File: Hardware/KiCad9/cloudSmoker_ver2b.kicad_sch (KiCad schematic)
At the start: 54 parts, among them J1 AudioJack2_SwitchT, J10 Conn_01x02_Pin, J11 Conn_01x02_Pin, J12 Conn_01x02_Pin, J2 AudioJack2_SwitchT, J3 AudioJack2_SwitchT, J4 AudioJack2_SwitchT, J5 Conn_01x02_Pin, J6 Conn_01x02_Pin, J7 Conn_01x02_Pin, J8 Conn_01x02_Pin, J9 Conn_01x02_Pin, Q1 BSS138, Q2 BSS138, SW1 TS-1088-AR02016, SW2 TS-1088-AR02016, U1 SRV05-4-P-T7, U2 GT-USB-7010ASV, U3 ESP32-C3-WROOM-02U-N4, U4 AMS1117-3_3, U5 SRV05-4-P-T7, U6 ADS1115IRUGR

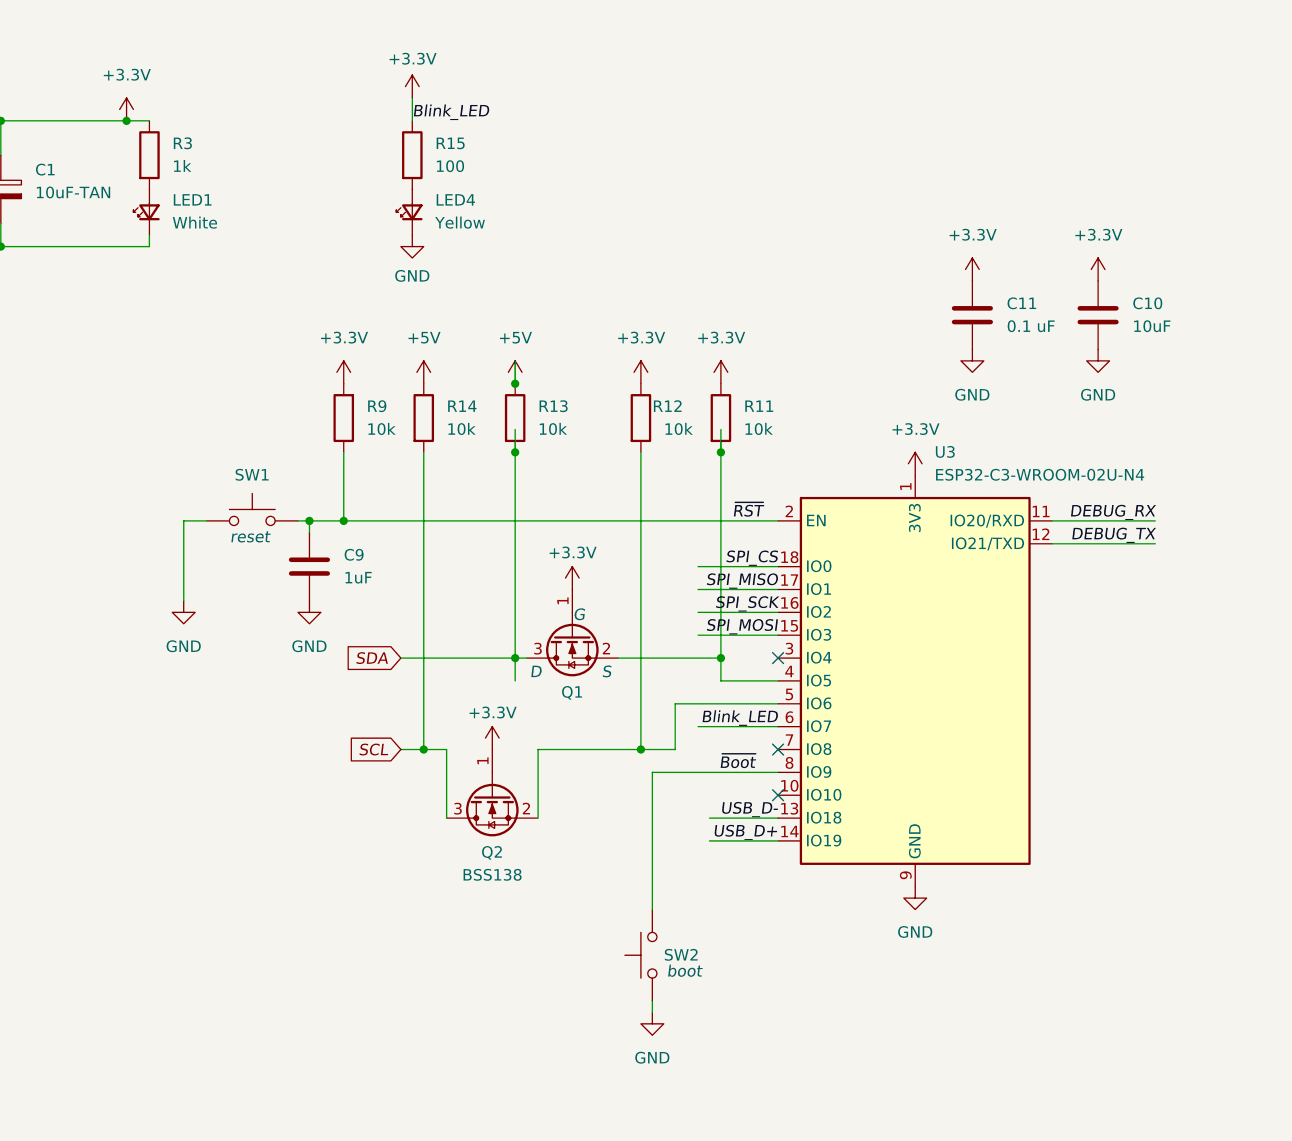
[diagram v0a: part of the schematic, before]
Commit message: cloudSmoker schematic ver2b changes
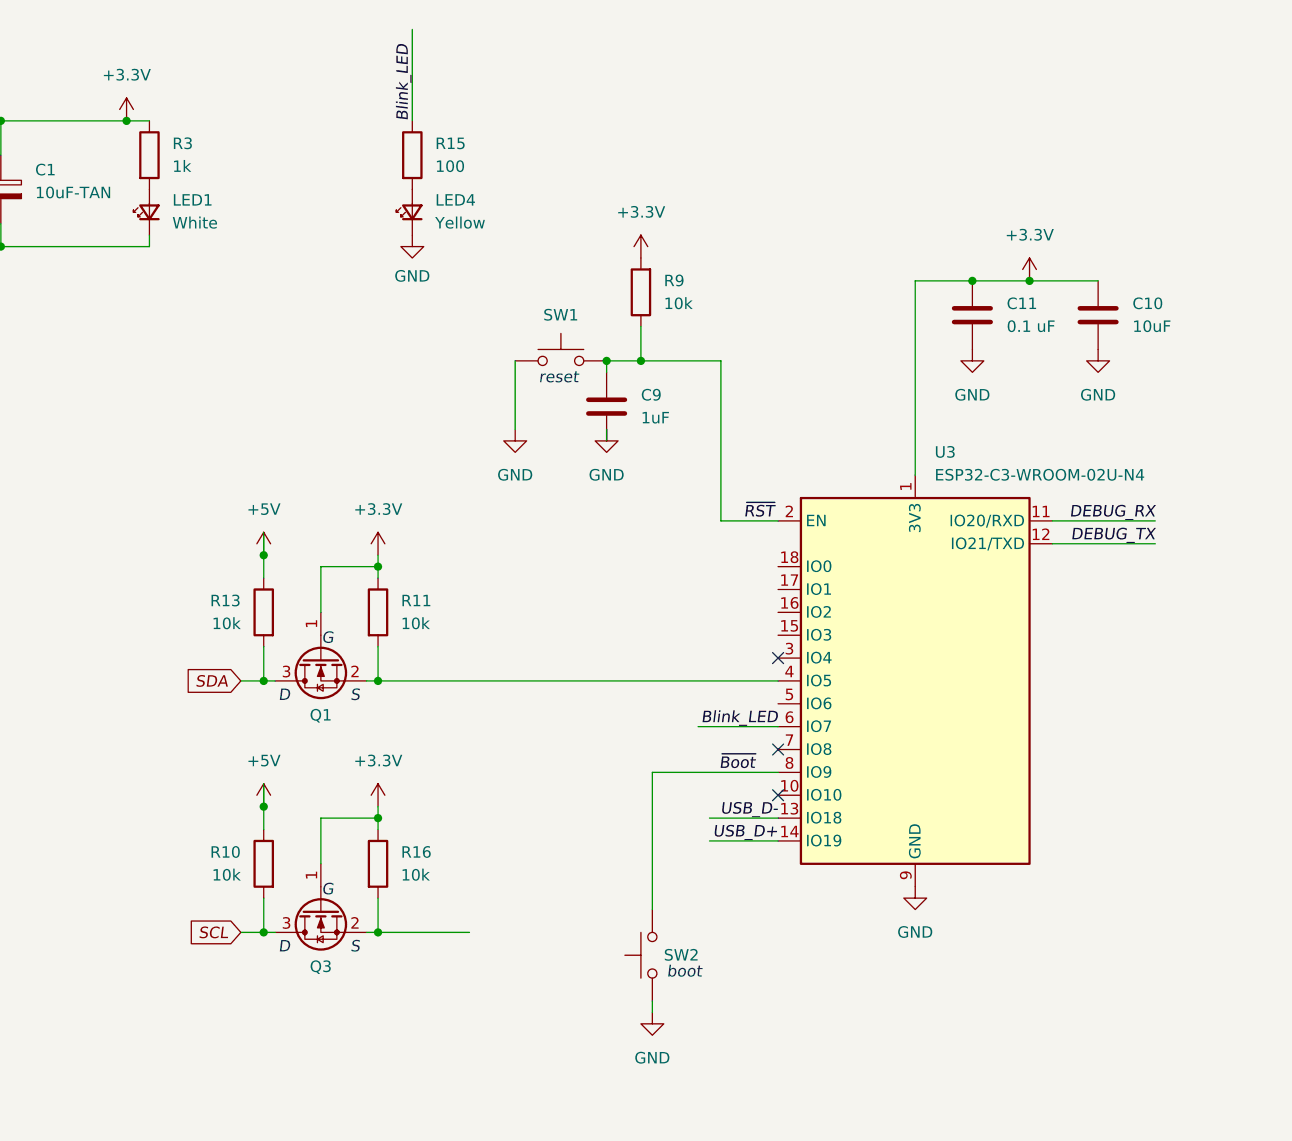
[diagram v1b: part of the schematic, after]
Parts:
- removed Q2: BSS138, Package_TO_SOT_SMD:SOT-23, symbol Transistor_FET:BSS138
- removed R12, R14: 10k, JLCImport:0603WAF1002T5E, symbol Device:R
- added Q3: BSS138, Package_TO_SOT_SMD:SOT-23, symbol Transistor_FET:BSS138
- added R10, R16: 10k, JLCImport:0603WAF1002T5E, symbol Device:R
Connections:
- net +3.3V: now also Q3.1 (G), R16.1; no longer R15.1, U3.6 (IO7)
- net +5V: now also R10.1
- net SCL: now also Q3.3 (D), R10.2
- net SPI_CS: no longer names the net of U3.18 (IO0)
- net SPI_MISO: no longer names the net of U3.17 (IO1)
- net SPI_MOSI: no longer names the net of U3.15 (IO3)
- net SPI_SCK: no longer names the net of U3.16 (IO2)
- new net: Q3.2 (S), R16.2
- new net Blink_LED: R15.1, U3.6 (IO7)
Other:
- moved on the sheet: C9, Q1, R11, R13, R9, SW1

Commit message: update schematic le:   Hardware/KiCad9/JLCImport.3dshapes/RLP25FEER100.step
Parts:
- removed C9: 1uF, JLCImport:CL10A105KB8NNNC, symbol Device:C
- removed J10, J11, J12, J5, J6, J7, J8: Conn_01x02_Pin, JST_XH_S2B-XH-A_1x02_P2.50mm_Horizontal, symbol Connector:Conn_01x02_Pin
- removed R9: 10k, JLCImport:0603WAF1002T5E, symbol Device:R
- removed SW1: TS-1088-AR02016, JLCImport:TS-1088-AR02016, symbol Switch:SW_Push
- added C11, C13: 100nF, JLCImport:CC0603KRX7R9BB104, symbol Device:C
- added C12: 1uF, JLCImport:CC0603KRX7R9BB104, symbol Device:C
- added FID1, FID2, FID3: Fiducial, symbol Mechanical:Fiducial
- added H1, H2, H3, H4: M3, symbol Mechanical:MountingHole_Pad
- added J10, J11, J8, J9: Conn_01x02_Pin, Connector_JST:JST_XH_B4B-XH-A_1x04_P2.50mm_Vertical, symbol Connector_Generic:Conn_01x04
- added J12: Conn_01x05, symbol Connector_Generic:Conn_01x05
- added J13: Conn_01x08, symbol Connector_Generic:Conn_01x08
- added J5, J6: Conn_01x04_Pin, Connector_JST:JST_XH_B4B-XH-A_1x04_P2.50mm_Vertical, symbol Connector_Generic:Conn_01x04
- added R14, R15, R16: 10k, JLCImport:0603WAF1002T5E, symbol Device:R
- added R17: 100 mOhm Shunt, JLCImport:RLP25FEER100, symbol Device:R_Shunt
- added SW2: TS-1088-AR02016, JLCImport:TS-1088-AR02016, symbol Switch:SW_Push
- added SW3: RotaryEncoder_Switch, symbol Device:RotaryEncoder_Switch
- added U7: INA226AIDGSR, Package_SO:VSSOP-10_3x3mm_P0.5mm, symbol Sensor_Energy:INA226
- C9: renamed from C11; value 0.1 uF -> 100nF
- J1, J2, J3, J4: now fitted
- J7: renamed from J9; footprint JST_XH_S2B-XH-A_1x02_P2.50mm_Horizontal -> Connector_JST:JST_XH_B4B-XH-A_1x04_P2.50mm_Vertical; symbol Connector:Conn_01x02_Pin -> Connector_Generic:Conn_01x04
- renumbered C4 to C1, C1 to C4, LED2 to LED1, LED1 to LED2, LED4 to LED3, Q3 to Q2, R5 to R1, R3 to R10, R7 to R11, R8 to R12, R15 to R13, R6 to R2, R4 to R3, R13 to R4, R11 to R5, R1 to R6, R10 to R7, R2 to R8, R16 to R9, SW2 to SW1, U2 to U1, U1 to U2, U4 to U3, U5 to U4, U3 to U5
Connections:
- net DEBUG_TX is gone; now on net DEBUG_TX/LED: U5.12 (IO21/TXD)
- net +3.3V: now also C13.1, J9.4 (Pin_4), R14.2, R15.2, R16.1, U7.6 (VS)
- net +5V: now also J11.2 (Pin_2), J12.5 (Pin_5), R17.4, U7.8 (Vbus); no longer C1.1, R3.1, U1.A4 (VBUS), U1.A9 (VBUS), U1.B4 (VBUS), U1.B9 (VBUS), U3.3 (VI)
- net DEBUG_RX: now also J9.3 (Pin_3)
- net GND: now also J7.3 (Pin_3), C11.2, C12.2, C13.2, H1.1, H2.1, H3.1, H4.1, J11.1 (Pin_1), J12.1 (Pin_1), J8.1 (Pin_1), J8.3 (Pin_3), J9.1 (Pin_1), SW2.1, U7.1 (A1), U7.2 (A0), U7.7 (GND)
- net at PR2.2, R8.2, U4.3 (IO2): now also J7.4 (Pin_4)
- net SDA_3V3: now reaches Q1.2 (S), R5.2
- net SDA_3V3: now also U5.15 (IO3), U5.16 (IO2), U7.4 (SDA), U7.5 (SCL); no longer U5.4 (IO5)
- net SCL_3V3: now reaches Q2.2 (S), R9.2
- net at PR3.2, R11.2, U4.4 (IO3): now also J8.2 (Pin_2)
- net DISP_CS: now reaches U5.10 (IO10)
- net DISP_CS: now also J10.3 (Pin_3)
- net ENC_SW: now reaches U5.17 (IO1)
- net ENC_SW: now also J12.4 (Pin_4)
- net DISP_BL: now reaches U5.18 (IO0)
- net DISP_BL: now also J10.4 (Pin_4)
- net ENC_CLK: now reaches U5.3 (IO4)
- net ENC_CLK: now also J12.2 (Pin_2)
- net SPI_SCK: now reaches U5.5 (IO6)
- net SPI_SCK: now also J11.3 (Pin_3)
- net DISP_DC: now reaches U5.7 (IO8)
- net DISP_DC: now also J10.2 (Pin_2), R16.2
- net at PR4.2, R12.2, U4.6 (IO4): now also J8.4 (Pin_4)
- net Blink_LED renamed DEBUG_TX/LED
- net DEBUG_TX/LED: now also J9.2 (Pin_2); no longer U5.6 (IO7)
- net JACK_TIP_MEAT1 renamed MEAT1
- net JACK_TIP_MEAT2 renamed MEAT2
- net JACK_TIP_MEAT3 renamed MEAT3
- net JACK_TIP_PIT renamed PIT
- net SCL renamed SCL_5V
- net SDA renamed SDA_5V
- net ~{Boot} renamed ~{BOOT}_DISP_RST
- net ~{BOOT}_DISP_RST: now also C11.1, J10.1 (Pin_1), R14.1
- net ~{RST} renamed ~{RESET}
- net ~{RESET}: now also C12.1, R15.1, SW2.2
- new net: R17.2, U7.10 (Vin+)
- new net: R17.3, U7.9 (Vin-)
- new net ENC_DT: J12.3 (Pin_3), U5.4 (IO5)
- new net SPI_MOSI: J11.4 (Pin_4), U5.6 (IO7)
- new net VBUS: C1.1, R17.1, R3.1, U1.A4 (VBUS), U1.A9 (VBUS), U1.B4 (VBUS), U1.B9 (VBUS), U3.3 (VI)
- no-connect marks 12 -> 39
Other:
- note added: ""Blink" Test LED"
- note added: "ADC 16-bit I2C"
- note added: "Boot Switch"
- note added: "Current Monitor (Powerbank State of Charge)"
- note added: "Display Header JST-XH"
- note added: "Display module has integrated transistor for Backlight control 3V3 logic signal safe"
- note added: "EC11 based Rotary Encoder Module"
- note added: "Encoder Header JST-XH"
- note added: "JST XH 4-pin Female (DNP - will add post-fabrication)"
- note added: "JST XH 4-pin Male"
- note added: "Logic Level Shifters Bidirrectional 5V <-> 3V3"
- note added: "Mechanical"
- note added: "Microcontroller"
- note added: "Place RC Filters close to ADC"
- note added: "Power Regulation"
- note added: "Reset Switch"
- note added: "Round Display GC9A01 1.28" TFT (3.3 - 5V compatible)"
- note added: "Slave Addrsss: 1000000b"
- note added: "Slave Addrsss: 1001000b"
- note added: "Switches"
- note added: "Thermistor Jacks Off-Board (Enclosure Panel Mounted)"
- note added: "Thermistors Bias / Low Pass Filter (16 Hz)"
- note added: "UART / Debug Header (JST-XH)"
- note added: "USB-C USB2.0 Flash / Power"
- note added: "User Interface (off-board - enclosure mounted)"
- note added: "User Interface Display / Rotary Encoder-Switch"
- note removed: "JST XH 2-pin Female"
- note removed: "JST XH 2-pin Male"
- note removed: "Thermistor Jacks - Off-Board (Panel Mounted)"
- note removed: "boot"
- note removed: "reset"
- moved on the sheet: C1, C10, C2, C3, C4, C5, C6, C7, C8, C9, LED1, LED2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
